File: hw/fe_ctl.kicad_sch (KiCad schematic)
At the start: 2 parts, among them U21 TCA6408A

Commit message: WIP - a lot already laid out.
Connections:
- net Vpp_analog renamed +5V_switched
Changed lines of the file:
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@@
     )
   )
-  (symbol (lib_id "fmc:Vpp_analog") (at 125.73 76.2 0) (unit 1)
+  (symbol (lib_id "fmc:+5V_switched") (at 125.73 76.2 0) (unit 1)
     (in_bom yes) (on_board yes) (dnp no)
-    (property "Reference" "#PWR032" (at 125.73 80.01 0)
+    (property "Reference" "#PWR09" (at 125.73 80.01 0)
       (effects (font (size 1.27 1.27)) hide)
     )
-    (property "Value" "Vpp_analog" (at 126.111 71.8058 0)
+    (property "Value" "+5V_switched" (at 125.73 71.755 0)
       (effects (font (size 1.27 1.27)))
     )
@@
     (instances
       (project "usbadc"
-        (path "/7c8a1f8d-8834-4c9b-aaae-1f231e9b09a1/00000000-0000-0000-0000-0000612b1274"
-          (reference "#PWR032") (unit 1)
+        (path "/7c8a1f8d-8834-4c9b-aaae-1f231e9b09a1/00000000-0000-0000-0000-00006086f2e3"
+          (reference "#PWR09") (unit 1)
         )
         (path "/7c8a1f8d-8834-4c9b-aaae-1f231e9b09a1/c969de1a-32a7-4770-b1aa-e527a627ef90/73f3d429-a0b7-4265-ba46-4445bae0de3d"
-          (reference "#PWR069") (unit 1)
+          (reference "#PWR033") (unit 1)
         )
       )

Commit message: finished routing; DRC passes (except for 1 hole violation at push-button)
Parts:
- R23: Manufacturer Yageo -> (none); Part RT0603FRE0710KL -> (none)
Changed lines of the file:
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@@
       (effects (font (size 1.27 1.27)) hide)
     )
-    (property "Part" "RT0603FRE0710KL" (at 111.76 88.9 90)
+    (property "Part" "" (at 111.76 88.9 90)
       (effects (font (size 1.27 1.27)) hide)
     )
-    (property "Manufacturer" "Yageo" (at 111.76 88.9 90)
+    (property "Manufacturer" "" (at 111.76 88.9 90)
       (effects (font (size 1.27 1.27)) hide)
     )

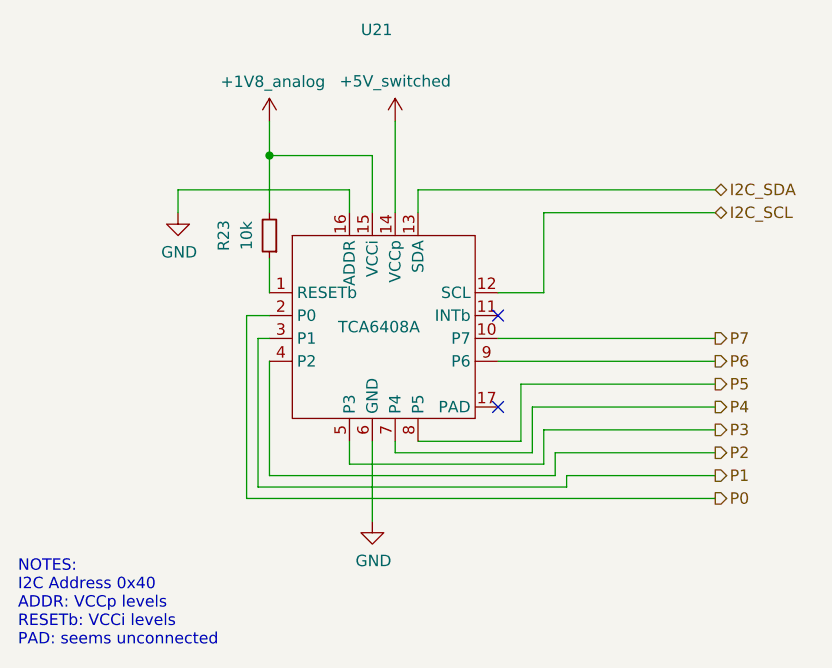
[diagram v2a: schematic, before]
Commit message: Added trion top-sheet as sub-sheet to usbadc project
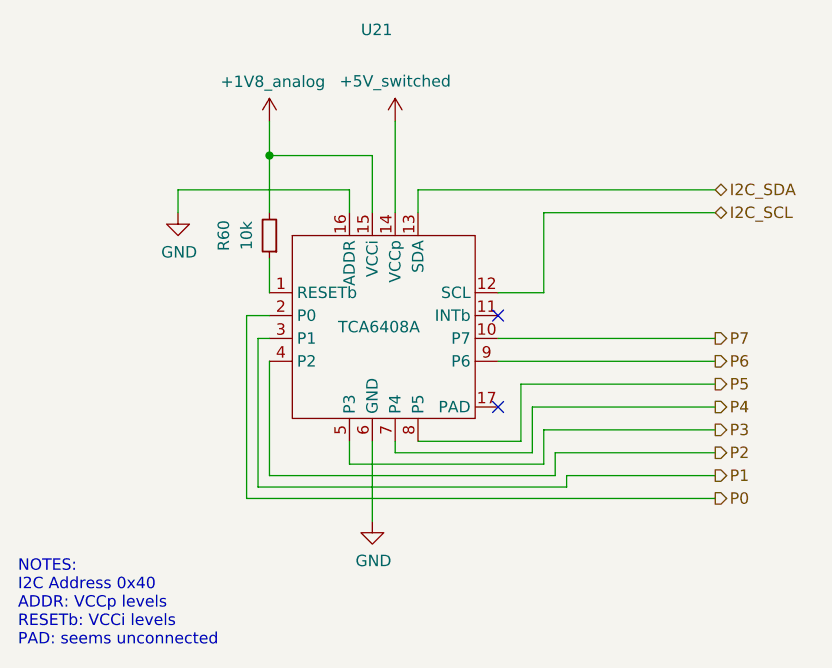
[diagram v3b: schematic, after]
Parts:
- renumbered R23 to R60
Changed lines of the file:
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@@
   (symbol (lib_id "power:GND") (at 101.6 86.36 0) (unit 1)
     (in_bom yes) (on_board yes) (dnp no)
-    (property "Reference" "#PWR033" (at 101.6 92.71 0)
+    (property "Reference" "#PWR066" (at 101.6 92.71 0)
       (effects (font (size 1.27 1.27)) hide)
     )
@@
     (instances
       (project "usbadc"
-        (path "/7c8a1f8d-8834-4c9b-aaae-1f231e9b09a1/00000000-0000-0000-0000-0000612b1274"
-          (reference "#PWR033") (unit 1)
-        )
-        (path "/7c8a1f8d-8834-4c9b-aaae-1f231e9b09a1/00000000-0000-0000-0000-000060b16d71"
-          (reference "#PWR?") (unit 1)
-        )
-        (path "/7c8a1f8d-8834-4c9b-aaae-1f231e9b09a1/00000000-0000-0000-0000-00006086f2e3"
-          (reference "#PWR?") (unit 1)
-        )
         (path "/7c8a1f8d-8834-4c9b-aaae-1f231e9b09a1/c969de1a-32a7-4770-b1aa-e527a627ef90/73f3d429-a0b7-4265-ba46-4445bae0de3d"
           (reference "#PWR066") (unit 1)
@@
   (symbol (lib_id "fmc:+1V8_analog") (at 111.76 76.2 0) (unit 1)
     (in_bom yes) (on_board yes) (dnp no)
-    (property "Reference" "#PWR034" (at 111.76 80.01 0)
+    (property "Reference" "#PWR067" (at 111.76 80.01 0)
       (effects (font (size 1.27 1.27)) hide)
     )
@@
     (instances
       (project "usbadc"
-        (path "/7c8a1f8d-8834-4c9b-aaae-1f231e9b09a1/00000000-0000-0000-0000-0000612b1274"
-          (reference "#PWR034") (unit 1)
-        )
         (path "/7c8a1f8d-8834-4c9b-aaae-1f231e9b09a1/c969de1a-32a7-4770-b1aa-e527a627ef90/73f3d429-a0b7-4265-ba46-4445bae0de3d"
           (reference "#PWR067") (unit 1)
@@
   (symbol (lib_id "fmc:+5V_switched") (at 125.73 76.2 0) (unit 1)
     (in_bom yes) (on_board yes) (dnp no)
-    (property "Reference" "#PWR09" (at 125.73 80.01 0)
+    (property "Reference" "#PWR033" (at 125.73 80.01 0)
       (effects (font (size 1.27 1.27)) hide)
     )
@@
     (instances
       (project "usbadc"
-        (path "/7c8a1f8d-8834-4c9b-aaae-1f231e9b09a1/00000000-0000-0000-0000-00006086f2e3"
-          (reference "#PWR09") (unit 1)
-        )
         (path "/7c8a1f8d-8834-4c9b-aaae-1f231e9b09a1/c969de1a-32a7-4770-b1aa-e527a627ef90/73f3d429-a0b7-4265-ba46-4445bae0de3d"
           (reference "#PWR033") (unit 1)
@@
   (symbol (lib_id "Device:R_Small") (at 111.76 88.9 180) (unit 1)
     (in_bom yes) (on_board yes) (dnp no)
-    (property "Reference" "R23" (at 106.68 88.9 90)
+    (property "Reference" "R60" (at 106.68 88.9 90)
       (effects (font (size 1.27 1.27)))
     )
@@
     (instances
       (project "usbadc"
-        (path "/7c8a1f8d-8834-4c9b-aaae-1f231e9b09a1/00000000-0000-0000-0000-000060b16d71"
-          (reference "R23") (unit 1)
-        )
         (path "/7c8a1f8d-8834-4c9b-aaae-1f231e9b09a1/c969de1a-32a7-4770-b1aa-e527a627ef90/73f3d429-a0b7-4265-ba46-4445bae0de3d"
           (reference "R60") (unit 1)
@@
   (symbol (lib_id "power:GND") (at 123.19 120.65 0) (unit 1)
     (in_bom yes) (on_board yes) (dnp no)
-    (property "Reference" "#PWR033" (at 123.19 127 0)
+    (property "Reference" "#PWR068" (at 123.19 127 0)
       (effects (font (size 1.27 1.27)) hide)
     )
@@
     (instances
       (project "usbadc"
-        (path "/7c8a1f8d-8834-4c9b-aaae-1f231e9b09a1/00000000-0000-0000-0000-0000612b1274"
-          (reference "#PWR033") (unit 1)
-        )
-        (path "/7c8a1f8d-8834-4c9b-aaae-1f231e9b09a1/00000000-0000-0000-0000-000060b16d71"
-          (reference "#PWR?") (unit 1)
-        )
-        (path "/7c8a1f8d-8834-4c9b-aaae-1f231e9b09a1/00000000-0000-0000-0000-00006086f2e3"
-          (reference "#PWR?") (unit 1)
-        )
         (path "/7c8a1f8d-8834-4c9b-aaae-1f231e9b09a1/c969de1a-32a7-4770-b1aa-e527a627ef90/73f3d429-a0b7-4265-ba46-4445bae0de3d"
           (reference "#PWR068") (unit 1)

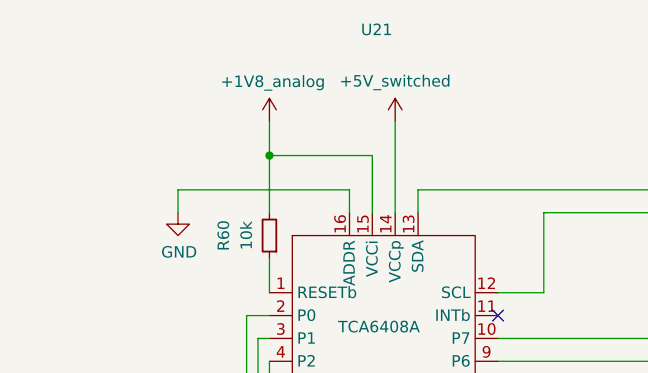
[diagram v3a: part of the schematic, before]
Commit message: rewired 1V8_analog to +2V5_analog
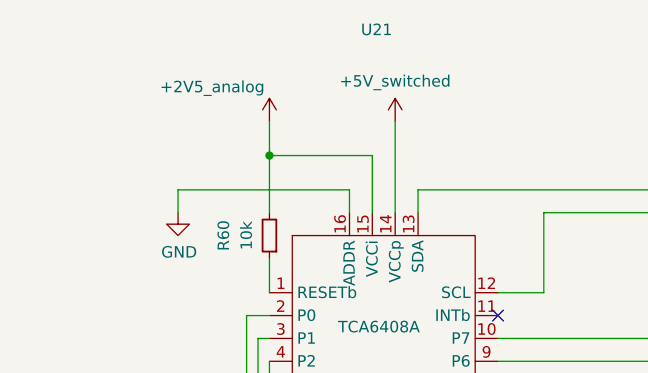
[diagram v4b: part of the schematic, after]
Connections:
- net +1V8_analog renamed +2V5_analog
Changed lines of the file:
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@@
     (effects (font (size 1.27 1.27)) (justify left))
+  )
+  (symbol (lib_id "fmc:+2V5_analog") (at 111.76 76.2 0) (mirror y) (unit 1)
+    (in_bom yes) (on_board yes) (dnp no)
+    (property "Reference" "#PWR067" (at 111.76 80.01 0)
+      (effects (font (size 1.27 1.27)) hide)
+    )
+    (property "Value" "+2V5_analog" (at 105.41 72.39 0)
+      (effects (font (size 1.27 1.27)))
+    )
+    (property "Footprint" "" (at 111.76 76.2 0)
+      (effects (font (size 1.27 1.27)) hide)
+    )
+    (property "Datasheet" "" (at 111.76 76.2 0)
+      (effects (font (size 1.27 1.27)) hide)
+    )
+    (pin "1")
+    (instances
+      (project "usbadc"
+        (path "/7c8a1f8d-8834-4c9b-aaae-1f231e9b09a1/c969de1a-32a7-4770-b1aa-e527a627ef90/73f3d429-a0b7-4265-ba46-4445bae0de3d"
+          (reference "#PWR067") (unit 1)
+        )
+      )
+    )
   )
   (symbol (lib_id "power:GND") (at 101.6 86.36 0) (unit 1)
@@
         )
       )
-    )
-  )
-  (symbol (lib_id "fmc:+1V8_analog") (at 111.76 76.2 0) (unit 1)
-    (in_bom yes) (on_board yes) (dnp no)
-    (property "Reference" "#PWR067" (at 111.76 80.01 0)
-      (effects (font (size 1.27 1.27)) hide)
-    )
-    (property "Value" "+1V8_analog" (at 112.141 71.8058 0)
-      (effects (font (size 1.27 1.27)))
-    )
-    (property "Footprint" "" (at 111.76 76.2 0)
-      (effects (font (size 1.27 1.27)) hide)
-    )
-    (property "Datasheet" "" (at 111.76 76.2 0)
-      (effects (font (size 1.27 1.27)) hide)
-    )
-    (pin "1")
-    (instances
-      (project "usbadc"
-        (path "/7c8a1f8d-8834-4c9b-aaae-1f231e9b09a1/c969de1a-32a7-4770-b1aa-e527a627ef90/73f3d429-a0b7-4265-ba46-4445bae0de3d"
-          (reference "#PWR067") (unit 1)
-        )
-      )

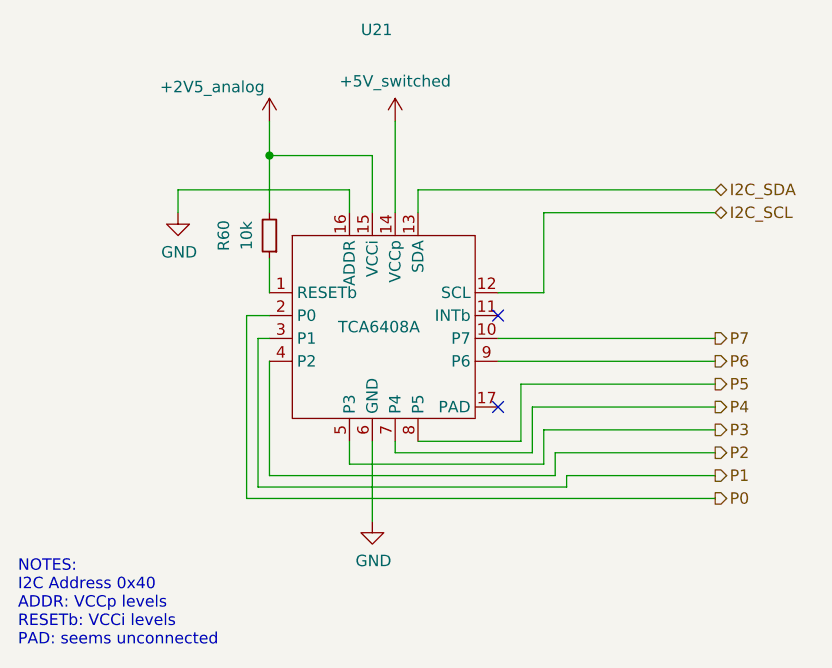
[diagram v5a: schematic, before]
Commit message: Connected FEC i2c to 3V3
This permits omitting the i2c level converted if the DAC is not used.
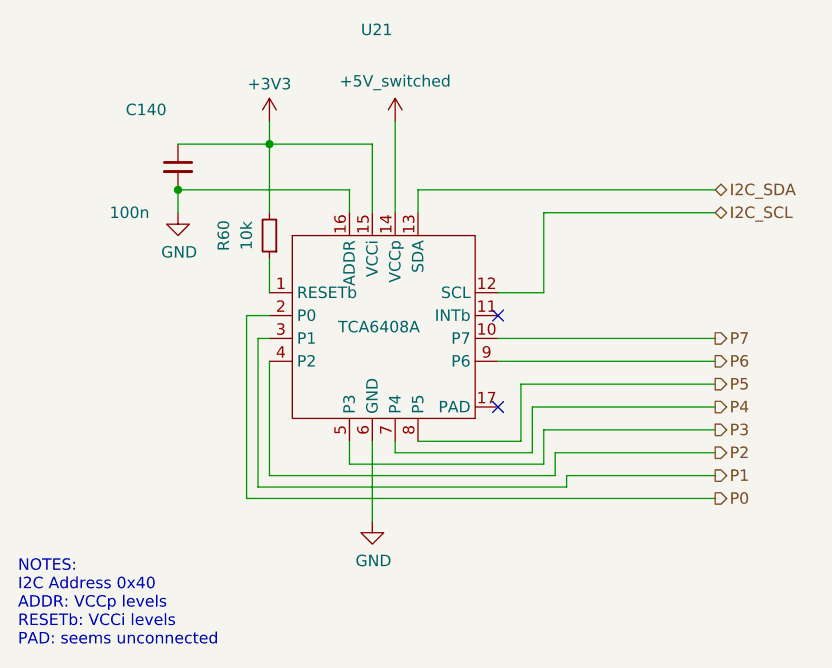
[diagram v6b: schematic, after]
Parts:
- added C140: 100n, Capacitor_SMD:C_0603_1608Metric, symbol Device:C_Small
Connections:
- net GND: now also C140.2
- net +2V5_analog renamed +3V3
- net +3V3: now also C140.1
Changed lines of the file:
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@@
 (kicad_sch (version 20230121) (generator eeschema)
   (paper "A4")
-  (junction (at 111.76 80.01) (diameter 0) (color 0 0 0 0)
+  (junction (at 111.76 78.74) (diameter 0) (color 0 0 0 0)
+  )
+  (junction (at 101.6 83.82) (diameter 0) (color 0 0 0 0)
   )
   (no_connect (at 137.16 107.95))
@@
     (stroke (width 0) (type default))
   )
-  (wire (pts (xy 123.19 80.01) (xy 123.19 86.36))
+  (wire (pts (xy 123.19 78.74) (xy 123.19 86.36))
     (stroke (width 0) (type default))
   )
@@
     (stroke (width 0) (type default))
   )
-  (wire (pts (xy 111.76 80.01) (xy 123.19 80.01))
+  (wire (pts (xy 111.76 78.74) (xy 123.19 78.74))
     (stroke (width 0) (type default))
   )
@@
     (stroke (width 0) (type default))
   )
-  (wire (pts (xy 111.76 80.01) (xy 111.76 86.36))
+  (wire (pts (xy 111.76 78.74) (xy 111.76 86.36))
     (stroke (width 0) (type default))
   )
@@
     (stroke (width 0) (type default))
   )
-  (wire (pts (xy 111.76 76.2) (xy 111.76 80.01))
+  (wire (pts (xy 111.76 76.2) (xy 111.76 78.74))
     (stroke (width 0) (type default))
   )
@@
   )
   (wire (pts (xy 120.65 114.3) (xy 142.24 114.3))
+    (stroke (width 0) (type default))
+  )
+  (wire (pts (xy 101.6 78.74) (xy 111.76 78.74))
     (stroke (width 0) (type default))
   )
@@
     (effects (font (size 1.27 1.27)) (justify left))
   )
-  (symbol (lib_id "fmc:+2V5_analog") (at 111.76 76.2 0) (mirror y) (unit 1)
+  (symbol (lib_id "power:GND") (at 101.6 86.36 0) (unit 1)
     (in_bom yes) (on_board yes) (dnp no)
+    (property "Reference" "#PWR066" (at 101.6 92.71 0)
+      (effects (font (size 1.27 1.27)) hide)
+    )
+    (property "Value" "GND" (at 101.727 90.7542 0)
+      (effects (font (size 1.27 1.27)))
+    )
+    (property "Footprint" "" (at 101.6 86.36 0)
+      (effects (font (size 1.27 1.27)) hide)
+    )
+    (property "Datasheet" "" (at 101.6 86.36 0)
+      (effects (font (size 1.27 1.27)) hide)
+    )
+    (pin "1")
+    (instances
+      (project "usbadc"
+        (path "/7c8a1f8d-8834-4c9b-aaae-1f231e9b09a1/c969de1a-32a7-4770-b1aa-e527a627ef90/73f3d429-a0b7-4265-ba46-4445bae0de3d"
+          (reference "#PWR066") (unit 1)
+        )
+      )
+    )
+  )
+  (symbol (lib_id "Device:C_Small") (at 101.6 81.28 0) (mirror y) (unit 1)
+    (in_bom yes) (on_board yes) (dnp no)
+    (property "Reference" "C140" (at 100.33 74.93 0)
+      (effects (font (size 1.27 1.27)) (justify left))
+    )
+    (property "Value" "100n" (at 98.425 86.36 0)
+      (effects (font (size 1.27 1.27)) (justify left))
+    )
+    (property "Footprint" "Capacitor_SMD:C_0603_1608Metric" (at 101.6 81.28 0)
+      (effects (font (size 1.27 1.27)) hide)
+    )
+    (property "Datasheet" "~" (at 101.6 81.28 0)
+      (effects (font (size 1.27 1.27)) hide)
+    )
+    (property "Part" "CL10B104KB8NFN" (at 98.425 76.2 0)
+      (effects (font (size 1.27 1.27)) hide)
+    )
+    (property "Manufacturer" "Samsung" (at 95.885 73.66 0)
+      (effects (font (size 1.27 1.27)) hide)
+    )
+    (pin "1")
+    (pin "2")
+    (instances
+      (project "usbadc"
+        (path "/7c8a1f8d-8834-4c9b-aaae-1f231e9b09a1/c969de1a-32a7-4770-b1aa-e527a627ef90/73f3d429-a0b7-4265-ba46-4445bae0de3d"
+          (reference "C140") (unit 1)
+        )
+      )
+    )
+  )
+  (symbol (lib_id "power:+3V3") (at 111.76 76.2 0) (unit 1)
+    (in_bom yes) (on_board yes) (dnp no) (fields_autoplaced)
     (property "Reference" "#PWR067" (at 111.76 80.01 0)
       (effects (font (size 1.27 1.27)) hide)
     )
-    (property "Value" "+2V5_analog" (at 105.41 72.39 0)
+    (property "Value" "+3V3" (at 111.76 72.0669 0)
       (effects (font (size 1.27 1.27)))
     )
@@
         )
       )
-    )
-  )
-  (symbol (lib_id "power:GND") (at 101.6 86.36 0) (unit 1)
-    (in_bom yes) (on_board yes) (dnp no)
-    (property "Reference" "#PWR066" (at 101.6 92.71 0)
-      (effects (font (size 1.27 1.27)) hide)
-    )
-    (property "Value" "GND" (at 101.727 90.7542 0)
-      (effects (font (size 1.27 1.27)))
-    )
-    (property "Footprint" "" (at 101.6 86.36 0)
-      (effects (font (size 1.27 1.27)) hide)
-    )
-    (property "Datasheet" "" (at 101.6 86.36 0)
-      (effects (font (size 1.27 1.27)) hide)
-    )
-    (pin "1")
-    (instances
-      (project "usbadc"
-        (path "/7c8a1f8d-8834-4c9b-aaae-1f231e9b09a1/c969de1a-32a7-4770-b1aa-e527a627ef90/73f3d429-a0b7-4265-ba46-4445bae0de3d"
-          (reference "#PWR066") (unit 1)
-        )
-      )

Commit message: Replaced 5V power switch by LDO.
Unregulated 5V introduced a LOT of noise into the FE.
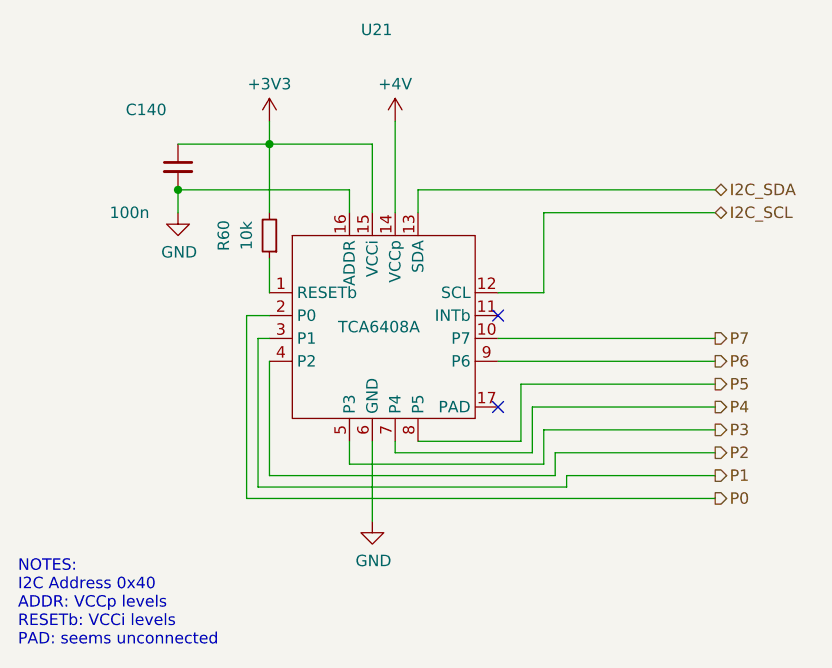
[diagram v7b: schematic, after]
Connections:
- net +5V_switched renamed +4V
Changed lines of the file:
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@@
     )
   )
-  (symbol (lib_id "fmc:+5V_switched") (at 125.73 76.2 0) (unit 1)
-    (in_bom yes) (on_board yes) (dnp no)
-    (property "Reference" "#PWR033" (at 125.73 80.01 0)
+  (symbol (lib_id "power:+4V") (at 125.73 76.2 0) (unit 1)
+    (in_bom yes) (on_board yes) (dnp no) (fields_autoplaced)
+    (property "Reference" "#PWR0126" (at 125.73 80.01 0)
       (effects (font (size 1.27 1.27)) hide)
     )
-    (property "Value" "+5V_switched" (at 125.73 71.755 0)
+    (property "Value" "+4V" (at 125.73 72.0669 0)
       (effects (font (size 1.27 1.27)))
     )
@@
       (project "usbadc"
         (path "/7c8a1f8d-8834-4c9b-aaae-1f231e9b09a1/c969de1a-32a7-4770-b1aa-e527a627ef90/73f3d429-a0b7-4265-ba46-4445bae0de3d"
-          (reference "#PWR033") (unit 1)
+          (reference "#PWR0126") (unit 1)
         )
       )
